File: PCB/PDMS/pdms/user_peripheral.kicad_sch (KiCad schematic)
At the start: 11 parts, among them IC12 TMP126NDCKR, IC14 TMP126NDCKR, Q2 RJU002N06FRAT106

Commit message: Final touch before PCB order
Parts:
- renumbered R65 to R57, R57 to R65
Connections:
- net MISO renamed SPI1_MISO
- net MOSI renamed SPI1_MOSI
- net SCK renamed SPI1_SCK
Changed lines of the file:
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@@
     (effects (font (size 1.27 1.27)) (justify left bottom))
   )
-  (label "SCK" (at 93.345 66.675 90)
-    (effects (font (size 1.27 1.27)) (justify left bottom))
-  )
-  (label "MOSI" (at 59.055 66.675 90)
-    (effects (font (size 1.27 1.27)) (justify left bottom))
-  )
-  (label "MISO" (at 55.245 66.675 90)
-    (effects (font (size 1.27 1.27)) (justify left bottom))
-  )
-  (label "MISO" (at 131.445 66.675 90)
-    (effects (font (size 1.27 1.27)) (justify left bottom))
-  )
-  (label "MOSI" (at 135.255 66.675 90)
-    (effects (font (size 1.27 1.27)) (justify left bottom))
-  )
-  (label "SCK" (at 169.545 66.675 90)
-    (effects (font (size 1.27 1.27)) (justify left bottom))
-  )
-  (global_label "{SPI3}" (shape input) (at 41.275 70.485 180) (fields_autoplaced)
+  (label "SPI1_SCK" (at 93.345 66.675 90)
+    (effects (font (size 1.27 1.27)) (justify left bottom))
+  )
+  (label "SPI1_MOSI" (at 59.055 66.675 90)
+    (effects (font (size 1.27 1.27)) (justify left bottom))
+  )
+  (label "SPI1_MISO" (at 55.245 66.675 90)
+    (effects (font (size 1.27 1.27)) (justify left bottom))
+  )
+  (label "SPI1_MISO" (at 131.445 66.675 90)
+    (effects (font (size 1.27 1.27)) (justify left bottom))
+  )
+  (label "SPI1_MOSI" (at 135.255 66.675 90)
+    (effects (font (size 1.27 1.27)) (justify left bottom))
+  )
+  (label "SPI1_SCK" (at 169.545 66.675 90)
+    (effects (font (size 1.27 1.27)) (justify left bottom))
+  )
+  (global_label "{SPI1}" (shape input) (at 41.275 70.485 180) (fields_autoplaced)
     (effects (font (size 1.27 1.27)) (justify right))
     (property "Intersheet References" "${INTERSHEET_REFS}" (id 0) (at 32.8748 70.4056 0)
@@
   (symbol (lib_id "power:+5V") (at 259.08 20.574 0) (unit 1)
     (in_bom yes) (on_board yes)
-    (property "Reference" "#PWR0200" (id 0) (at 259.08 24.384 0)
+    (property "Reference" "#PWR0197" (id 0) (at 259.08 24.384 0)
       (effects (font (size 0.8 0.8)) hide)
     )
@@
   (symbol (lib_id "power:GND") (at 259.08 48.26 0) (unit 1)
     (in_bom yes) (on_board yes)
-    (property "Reference" "#PWR0199" (id 0) (at 259.08 54.61 0)
+    (property "Reference" "#PWR0196" (id 0) (at 259.08 54.61 0)
       (effects (font (size 0.8 0.8)) hide)
     )
@@
   (symbol (lib_id "Device:R_Small") (at 102.235 47.625 0) (unit 1)
     (in_bom yes) (on_board yes) (fields_autoplaced)
-    (property "Reference" "R65" (id 0) (at 104.775 46.3549 0)
+    (property "Reference" "R57" (id 0) (at 104.775 46.3549 0)
       (effects (font (size 0.8 0.8)) (justify left))
     )
@@
   (symbol (lib_id "power:GND") (at 169.545 38.735 180) (unit 1)
     (in_bom yes) (on_board yes) (fields_autoplaced)
-    (property "Reference" "#PWR0309" (id 0) (at 169.545 32.385 0)
+    (property "Reference" "#PWR0194" (id 0) (at 169.545 32.385 0)
       (effects (font (size 1.27 1.27)) hide)
     )
@@
   (symbol (lib_id "power:GND") (at 61.595 51.435 270) (unit 1)
     (in_bom yes) (on_board yes) (fields_autoplaced)
-    (property "Reference" "#PWR0195" (id 0) (at 55.245 51.435 0)
+    (property "Reference" "#PWR0233" (id 0) (at 55.245 51.435 0)
       (effects (font (size 0.8 0.8)) hide)
     )
@@
   (symbol (lib_id "power:+3.3V") (at 95.25 48.895 270) (unit 1)
     (in_bom yes) (on_board yes) (fields_autoplaced)
-    (property "Reference" "#PWR0194" (id 0) (at 91.44 48.895 0)
+    (property "Reference" "#PWR0309" (id 0) (at 91.44 48.895 0)
       (effects (font (size 0.8 0.8)) hide)
     )
@@
   (symbol (lib_id "power:+3.3V") (at 170.815 48.895 270) (unit 1)
     (in_bom yes) (on_board yes) (fields_autoplaced)
-    (property "Reference" "#PWR0233" (id 0) (at 167.005 48.895 0)
+    (property "Reference" "#PWR0199" (id 0) (at 167.005 48.895 0)
       (effects (font (size 0.8 0.8)) hide)
     )
@@
   (symbol (lib_id "power:GND") (at 93.345 38.735 180) (unit 1)
     (in_bom yes) (on_board yes) (fields_autoplaced)
-    (property "Reference" "#PWR0310" (id 0) (at 93.345 32.385 0)
+    (property "Reference" "#PWR0239" (id 0) (at 93.345 32.385 0)
       (effects (font (size 1.27 1.27)) hide)
     )
@@
   (symbol (lib_id "Device:R_Small") (at 135.255 57.785 0) (unit 1)
     (in_bom yes) (on_board yes)
-    (property "Reference" "R57" (id 0) (at 136.525 56.515 0)
+    (property "Reference" "R65" (id 0) (at 136.525 56.515 0)
       (effects (font (size 1.27 1.27)) (justify left))
     )
@@
   (symbol (lib_id "power:GND") (at 137.795 51.435 270) (unit 1)
     (in_bom yes) (on_board yes) (fields_autoplaced)
-    (property "Reference" "#PWR0196" (id 0) (at 131.445 51.435 0)
+    (property "Reference" "#PWR0195" (id 0) (at 131.445 51.435 0)
       (effects (font (size 0.8 0.8)) hide)
     )
@@
   (symbol (lib_id "power:+3.3V") (at 102.235 43.815 0) (unit 1)
     (in_bom yes) (on_board yes) (fields_autoplaced)
-    (property "Reference" "#PWR0197" (id 0) (at 102.235 47.625 0)
+    (property "Reference" "#PWR0310" (id 0) (at 102.235 47.625 0)
       (effects (font (size 0.8 0.8)) hide)
     )
@@
   (symbol (lib_id "power:+3.3V") (at 178.435 43.815 0) (unit 1)
     (in_bom yes) (on_board yes) (fields_autoplaced)
-    (property "Reference" "#PWR0239" (id 0) (at 178.435 47.625 0)
-      (effects (font (size 0.8 0.8)) hide)
-    )
+    (property "Reference" "#PWR0200" (id 0) (at 178.435 47.625 0)
+      (effects (font (size 0.8 0.8)) hide)
+    )

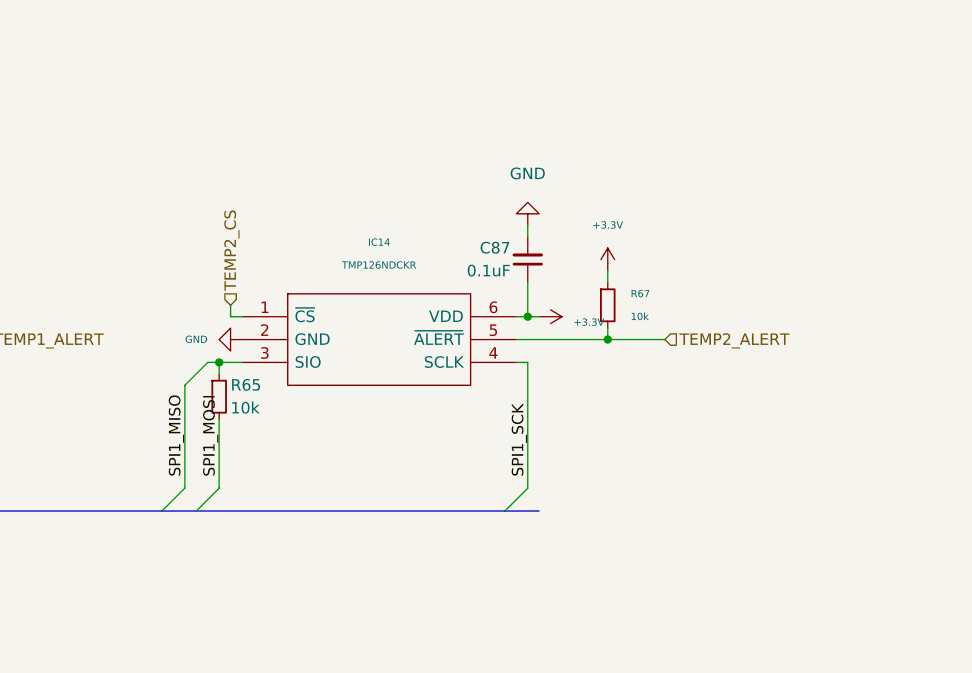
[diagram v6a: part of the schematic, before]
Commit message: Changed main power connector, added USB-C, added BLE - not wired yet
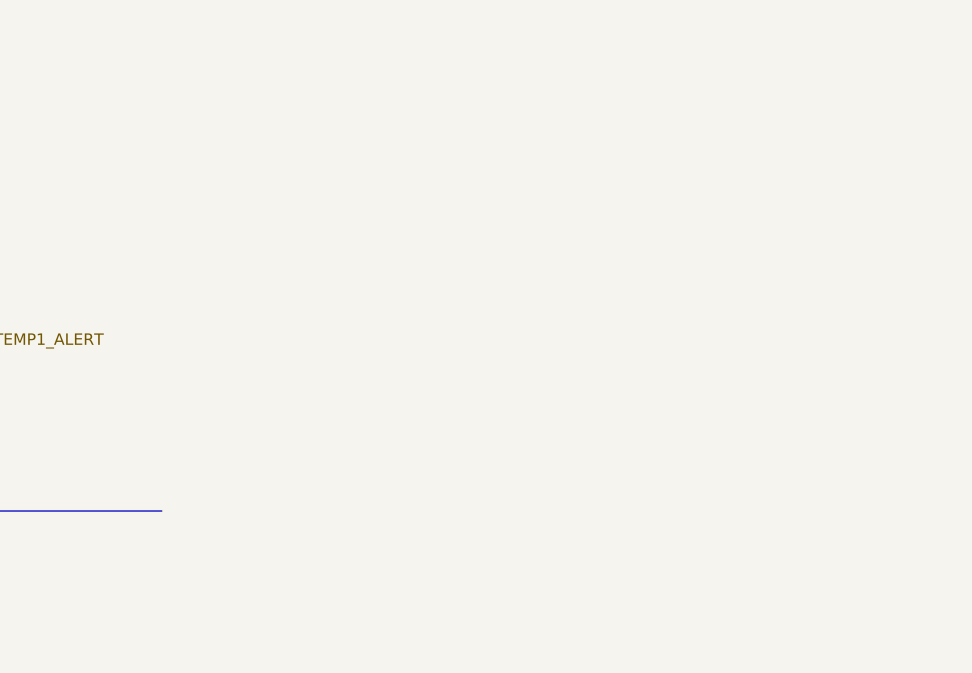
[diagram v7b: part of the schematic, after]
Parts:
- removed C87: 0.1uF, Capacitor_SMD:C_0402_1005Metric, symbol Device:C_Small
- removed IC14: TMP126NDCKR, PDM_Additional:SOT65P210X110-6N, symbol PDM_additional:TMP126NDCKR
- removed R65, R67: 10k, Resistor_SMD:R_0402_1005Metric, symbol Device:R_Small
